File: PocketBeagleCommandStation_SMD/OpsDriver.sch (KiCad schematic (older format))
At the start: 0 parts

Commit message: Working on PocketBeagleCommandStation_SMD.
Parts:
- added C?: 47 nf, symbol C_Small
- added C?: 1 uf, symbol C_Small
- added C? (x2): 100 nf, symbol C
- added C?: 47 uf, symbol CP1
- added C?: 1 uf, symbol C
- added R?: 0.005 Ohms, symbol R
- added R? (x3): 10K Ohms, symbol R
- added U?: DRV8873HPWPR, SOP65P640X120-25N, symbol DRV8873HPWPR
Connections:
- net A: now also U?.18 (OUT1_1), U?.19 (OUT1_2)
- net B: now also U?.14 (OUT2_1), U?.15 (OUT2_2)
- net BRAKE: now also U?.9 (DISABLE)
- net ENABLE: now also U?.7 (EN/IN1)
- net PowerIn: now also R?.1
- net SIGNAL: now also U?.8 (PH/IN2)
- new net: C?.1, U?.1 (DVDD), U?.6 (NOL)
- new net: R?.2, U?.11 (NSLEEP)
- new net: R?.2, U?.2 (NFAULT)
- new net: C?.2, U?.21 (VCP)
- new net: C?.2, U?.22 (CPH)
- new net: C?.1, U?.23 (CPL)
- new net: R?.1, U?.3 (MODE)
- new net +3V3: R?.1, R?.1
- new net GND: C?.2, C?.2, C?.2, C?.2, R?.2, U?.16 (SRC_1), U?.17 (SRC_2), U?.24 (GND), U?.25 (EP), U?.4 (SR), U?.5 (NITRIP)
- new net Sense_Neg: C?.1, C?.1, C?.1, C?.1, R?.2, U?.13 (VM_1), U?.20 (VM_2)
- no-connect marks 0 -> 2

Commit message: Continuing work on PocketBeagleCommandStation_SMD.
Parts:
- U4: renamed from U?; footprint SOP65P640X120-25N -> SOP65P640X120:SOP65P640X120-25N
- gave numbers to parts that had none: 10
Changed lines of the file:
@@
 LIBS:DRV8873HPWPR
 LIBS:DRV8801PWP
+LIBS:74ahc1g08
+LIBS:mcp9701at
 LIBS:PocketBeagleCommandStation_SMD-cache
 EELAYER 25 0
@@
 Sense_Neg
 $Comp
-L DRV8873HPWPR U?
+L DRV8873HPWPR U4
 U 1 1 606FD60F
 P 3550 1800
-F 0 "U?" H 4800 2100 50  0000 L CNN
+F 0 "U4" H 4800 2100 50  0000 L CNN
 F 1 "DRV8873HPWPR" H 4800 2000 50  0000 L CNN
-F 2 "SOP65P640X120-25N" H 4800 1900 50  0001 L CNN
+F 2 "SOP65P640X120:SOP65P640X120-25N" H 4800 1900 50  0001 L CNN
 F 3 "http://www.ti.com/lit/ds/symlink/drv8873.pdf" H 4800 1800 50  0001 L CNN
 F 4 "Motor / Motion / Ignition Controllers & Drivers 10A H-Bridge Motor Driver with Integrated Current Sensing and Current Sense Output" H 4800 1700 50  0001 L CNN "Description"
@@
 $EndComp
 $Comp
-L GND #PWR?
+L GND #PWR028
 U 1 1 6070432B
 P 5250 1800
-F 0 "#PWR?" H 5250 1550 50  0001 C CNN
+F 0 "#PWR028" H 5250 1550 50  0001 C CNN
 F 1 "GND" H 5250 1650 50  0000 C CNN
 F 2 "" H 5250 1800 50  0001 C CNN
@@
 $EndComp
 $Comp
-L GND #PWR?
+L GND #PWR029
 U 1 1 60704370
 P 4250 3550
-F 0 "#PWR?" H 4250 3300 50  0001 C CNN
+F 0 "#PWR029" H 4250 3300 50  0001 C CNN
 F 1 "GND" H 4250 3400 50  0000 C CNN
 F 2 "" H 4250 3550 50  0001 C CNN
@@
 $EndComp
 $Comp
-L R R?
+L R R17
 U 1 1 607043BF
 P 5800 1550
-F 0 "R?" V 5880 1550 50  0000 C CNN
+F 0 "R17" V 5880 1550 50  0000 C CNN
 F 1 "0.005 Ohms" V 5800 1550 50  0000 C CNN
 F 2 "" V 5730 1550 50  0001 C CNN
@@
 Local_VDD
 $Comp
-L C_Small C?
+L C_Small C11
 U 1 1 607044D9
 P 5100 1950
-F 0 "C?" H 5110 2020 50  0000 L CNN
+F 0 "C11" H 5110 2020 50  0000 L CNN
 F 1 "47 nf" H 5110 1870 50  0000 L CNN
 F 2 "" H 5100 1950 50  0001 C CNN
@@
 $EndComp
 $Comp
-L C_Small C?
+L C_Small C12
 U 1 1 6070454C
 P 5250 2100
-F 0 "C?" H 5260 2170 50  0000 L CNN
+F 0 "C12" H 5260 2170 50  0000 L CNN
 F 1 "1 uf" H 5260 2020 50  0000 L CNN
 F 2 "" H 5250 2100 50  0001 C CNN
@@
 $EndComp
 $Comp
-L C C?
+L C C13
 U 1 1 607045D9
 P 5800 2450
-F 0 "C?" H 5825 2550 50  0000 L CNN
+F 0 "C13" H 5825 2550 50  0000 L CNN
 F 1 "100 nf" H 5825 2350 50  0000 L CNN
 F 2 "" H 5838 2300 50  0001 C CNN
@@
 $EndComp
 $Comp
-L C C?
+L C C14
 U 1 1 607045FC
 P 6150 2450
-F 0 "C?" H 6175 2550 50  0000 L CNN
+F 0 "C14" H 6175 2550 50  0000 L CNN
 F 1 "100 nf" H 6175 2350 50  0000 L CNN
 F 2 "" H 6188 2300 50  0001 C CNN
@@
 $EndComp
 $Comp
-L CP1 C?
+L CP1 C15
 U 1 1 60704621
 P 6500 2450
-F 0 "C?" H 6525 2550 50  0000 L CNN
+F 0 "C15" H 6525 2550 50  0000 L CNN
 F 1 "47 uf" H 6525 2350 50  0000 L CNN
 F 2 "" H 6500 2450 50  0001 C CNN
@@
 $EndComp
 $Comp
-L GND #PWR?
+L GND #PWR030
 U 1 1 60704783
 P 6150 2750
-F 0 "#PWR?" H 6150 2500 50  0001 C CNN
+F 0 "#PWR030" H 6150 2500 50  0001 C CNN
 F 1 "GND" H 6150 2600 50  0000 C CNN
 F 2 "" H 6150 2750 50  0001 C CNN
@@
 $EndComp
 $Comp
-L GND #PWR?
+L GND #PWR031
 U 1 1 60704831
 P 5300 2550
-F 0 "#PWR?" H 5300 2300 50  0001 C CNN
+F 0 "#PWR031" H 5300 2300 50  0001 C CNN
 F 1 "GND" H 5300 2400 50  0000 C CNN
 F 2 "" H 5300 2550 50  0001 C CNN
@@
 NoConn ~ 3550 2900
 $Comp
-L C C?
+L C C10
 U 1 1 607048DD
 P 3000 2000
-F 0 "C?" H 3025 2100 50  0000 L CNN
+F 0 "C10" H 3025 2100 50  0000 L CNN
 F 1 "1 uf" H 3025 1900 50  0000 L CNN
 F 2 "" H 3038 1850 50  0001 C CNN
@@
 $EndComp
 $Comp
-L GND #PWR?
+L GND #PWR032
 U 1 1 6070495B
 P 3000 2250
-F 0 "#PWR?" H 3000 2000 50  0001 C CNN
+F 0 "#PWR032" H 3000 2000 50  0001 C CNN
 F 1 "GND" H 3000 2100 50  0000 C CNN
 F 2 "" H 3000 2250 50  0001 C CNN
@@
 $EndComp
 $Comp
-L R R?
+L R R16
 U 1 1 60704A49
 P 3500 1450
-F 0 "R?" V 3580 1450 50  0000 C CNN
+F 0 "R16" V 3580 1450 50  0000 C CNN
 F 1 "10K Ohms" V 3500 1450 50  0000 C CNN
 F 2 "" V 3430 1450 50  0001 C CNN
@@
 $EndComp
 $Comp
-L R R?
+L R R15
 U 1 1 60704A7E
 P 3400 1450
-F 0 "R?" V 3480 1450 50  0000 C CNN
+F 0 "R15" V 3480 1450 50  0000 C CNN
 F 1 "10K Ohms" V 3400 1450 50  0000 C CNN
 F 2 "" V 3330 1450 50  0001 C CNN
@@
 $EndComp
 $Comp
-L +3.3V #PWR?
+L +3.3V #PWR033
 U 1 1 60707495
 P 3400 1100
-F 0 "#PWR?" H 3400 950 50  0001 C CNN
+F 0 "#PWR033" H 3400 950 50  0001 C CNN
 F 1 "+3.3V" H 3400 1240 50  0000 C CNN
 F 2 "" H 3400 1100 50  0001 C CNN
@@
 $EndComp
 $Comp
-L R R?
+L R R14
 U 1 1 6070758B
 P 2600 2150
-F 0 "R?" V 2680 2150 50  0000 C CNN
+F 0 "R14" V 2680 2150 50  0000 C CNN
 F 1 "10K Ohms" V 2600 2150 50  0000 C CNN
 F 2 "" V 2530 2150 50  0001 C CNN
@@
 $EndComp
 $Comp
-L GND #PWR?
+L GND #PWR034
 U 1 1 607075FE
 P 2600 2850
-F 0 "#PWR?" H 2600 2600 50  0001 C CNN
+F 0 "#PWR034" H 2600 2600 50  0001 C CNN
 F 1 "GND" H 2600 2700 50  0000 C CNN
 F 2 "" H 2600 2850 50  0001 C CNN
@@
 	5100 2350 5000 2350
 Wire Wire Line
-	5000 2300 5000 2350
-Wire Wire Line
-	5000 2350 5000 2400
+	5000 2300 5000 2400
 Wire Wire Line
 	5000 2300 4950 2300
@@
 	5100 2750 5000 2750
 Wire Wire Line
-	5000 2700 5000 2750
-Wire Wire Line
-	5000 2750 5000 2800
+	5000 2700 5000 2800
 Wire Wire Line
 	5000 2700 4950 2700
@@
 Connection ~ 5000 2750
 Wire Wire Line
-	4950 2200 5550 2200
-Wire Wire Line
-	5550 2200 5650 2200
-Wire Wire Line
-	5550 2200 5550 2300
-Wire Wire Line
-	5550 2300 5550 2900
+	5650 2200 4950 2200
+Wire Wire Line
+	5550 2200 5550 2900
 Wire Wire Line
 	5550 2900 4950 2900
@@
 	4250 3400 4250 3550
 Wire Wire Line
-	6050 1550 6000 1550
-Wire Wire Line
-	6000 1550 5950 1550
-Wire Wire Line
-	5650 2200 5650 2100
-Wire Wire Line
-	5650 2100 5650 1950
-Wire Wire Line
-	5650 1950 5650 1550
+	5950 1550 6050 1550
+Wire Wire Line
+	5650 1550 5650 2200
 Connection ~ 5550 2200
 Wire Wire Line
@@
 Connection ~ 5650 2100
 Wire Wire Line
-	5550 2300 5800 2300
-Wire Wire Line
-	5800 2300 6150 2300
-Wire Wire Line
-	6150 2300 6500 2300
+	5550 2300 6500 2300
 Connection ~ 6150 2300
 Connection ~ 5550 2300
 Connection ~ 5800 2300
 Wire Wire Line
-	5800 2600 6150 2600
-Wire Wire Line
-	6150 2600 6500 2600
+	5800 2600 6500 2600
 Connection ~ 6150 2600
 Wire Wire Line
@@
 	4950 2500 5050 2500
 Wire Wire Line
-	5050 2500 5050 2550
-Wire Wire Line
-	5050 2550 5050 2600
+	5050 2500 5050 2600
 Wire Wire Line
 	5050 2600 4950 2600
@@
 Connection ~ 5050 2550
 Wire Wire Line
-	3000 1800 3250 1800
-Wire Wire Line
-	3250 1800 3550 1800
+	3000 1800 3550 1800
 Wire Wire Line
 	3250 1800 3250 2300
@@
 Connection ~ 3250 1800
 Wire Wire Line
-	3000 2150 3000 2200
-Wire Wire Line
-	3000 2200 3000 2250
+	3000 2150 3000 2250
 Wire Wire Line
 	3500 1600 3500 1900
@@
 	3400 2800 3550 2800
 Wire Wire Line
-	3400 1100 3400 1150
-Wire Wire Line
-	3400 1150 3400 1300
+	3400 1100 3400 1300
 Wire Wire Line
 	3500 1300 3500 1150
@@
 	3450 2100 3450 2200
 Wire Wire Line
-	3000 2200 3450 2200
-Wire Wire Line
-	3450 2200 3550 2200
+	3000 2200 3550 2200
 Connection ~ 3000 2200
 Connection ~ 3450 2200

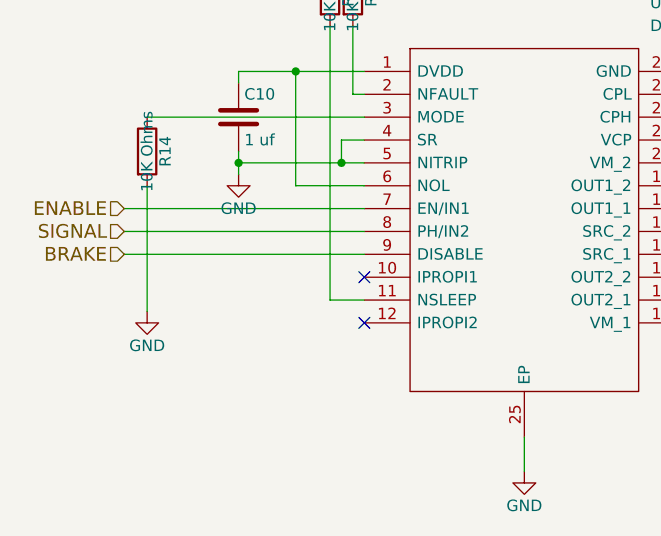
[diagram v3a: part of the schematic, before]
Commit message: Continuing work on the SMD version of PocketBeagleCommandStation.
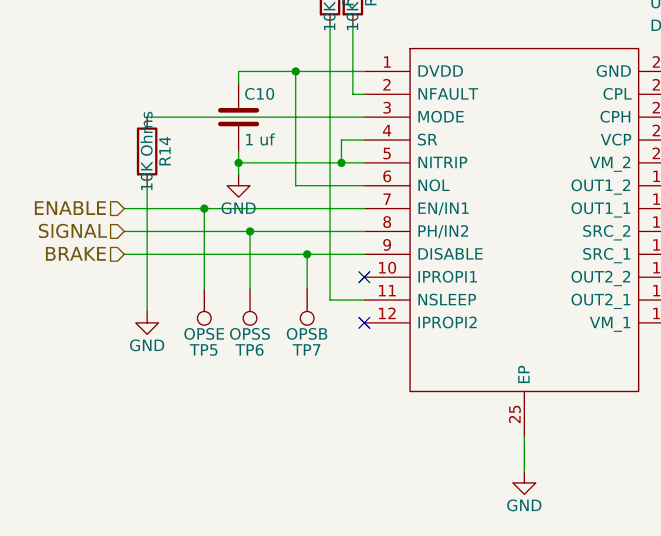
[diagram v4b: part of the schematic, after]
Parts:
- added TP5: OPSE, symbol TEST_1P
- added TP6: OPSS, symbol TEST_1P
- added TP7: OPSB, symbol TEST_1P
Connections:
- net BRAKE: now also TP7.1
- net ENABLE: now also TP5.1
- net SIGNAL: now also TP6.1
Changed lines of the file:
@@
 LIBS:74ahc1g08
 LIBS:mcp9701at
+LIBS:INA2180A1IDGKR
 LIBS:PocketBeagleCommandStation_SMD-cache
 EELAYER 25 0
@@
 $EndComp
 $Comp
-L GND #PWR028
+L GND #PWR37
 U 1 1 6070432B
 P 5250 1800
-F 0 "#PWR028" H 5250 1550 50  0001 C CNN
+F 0 "#PWR37" H 5250 1550 50  0001 C CNN
 F 1 "GND" H 5250 1650 50  0000 C CNN
 F 2 "" H 5250 1800 50  0001 C CNN
@@
 $EndComp
 $Comp
-L GND #PWR029
+L GND #PWR36
 U 1 1 60704370
 P 4250 3550
-F 0 "#PWR029" H 4250 3300 50  0001 C CNN
+F 0 "#PWR36" H 4250 3300 50  0001 C CNN
 F 1 "GND" H 4250 3400 50  0000 C CNN
 F 2 "" H 4250 3550 50  0001 C CNN
@@
 $EndComp
 $Comp
-L GND #PWR030
+L GND #PWR39
 U 1 1 60704783
 P 6150 2750
-F 0 "#PWR030" H 6150 2500 50  0001 C CNN
+F 0 "#PWR39" H 6150 2500 50  0001 C CNN
 F 1 "GND" H 6150 2600 50  0000 C CNN
 F 2 "" H 6150 2750 50  0001 C CNN
@@
 $EndComp
 $Comp
-L GND #PWR031
+L GND #PWR38
 U 1 1 60704831
 P 5300 2550
-F 0 "#PWR031" H 5300 2300 50  0001 C CNN
+F 0 "#PWR38" H 5300 2300 50  0001 C CNN
 F 1 "GND" H 5300 2400 50  0000 C CNN
 F 2 "" H 5300 2550 50  0001 C CNN
@@
 $EndComp
 $Comp
-L GND #PWR032
+L GND #PWR34
 U 1 1 6070495B
 P 3000 2250
-F 0 "#PWR032" H 3000 2000 50  0001 C CNN
+F 0 "#PWR34" H 3000 2000 50  0001 C CNN
 F 1 "GND" H 3000 2100 50  0000 C CNN
 F 2 "" H 3000 2250 50  0001 C CNN
@@
 $EndComp
 $Comp
-L +3.3V #PWR033
+L +3.3V #PWR35
 U 1 1 60707495
 P 3400 1100
-F 0 "#PWR033" H 3400 950 50  0001 C CNN
+F 0 "#PWR35" H 3400 950 50  0001 C CNN
 F 1 "+3.3V" H 3400 1240 50  0000 C CNN
 F 2 "" H 3400 1100 50  0001 C CNN
@@
 $EndComp
 $Comp
-L GND #PWR034
+L GND #PWR33
 U 1 1 607075FE
 P 2600 2850
-F 0 "#PWR034" H 2600 2600 50  0001 C CNN
+F 0 "#PWR33" H 2600 2600 50  0001 C CNN
 F 1 "GND" H 2600 2700 50  0000 C CNN
 F 2 "" H 2600 2850 50  0001 C CNN
@@
 	1    0    0    -1
 $EndComp
+$Comp
+L TEST_1P TP7
+U 1 1 60742F6B
+P 3300 2750
+F 0 "TP7" H 3300 3020 50  0000 C CNN
+F 1 "OPSB" H 3300 2950 50  0000 C CNN
+F 2 "" H 3500 2750 50  0001 C CNN
+F 3 "" H 3500 2750 50  0001 C CNN
+	1    3300 2750
+	-1   0    0    1
+$EndComp
+$Comp
+L TEST_1P TP6
+U 1 1 60743082
+P 3050 2750
+F 0 "TP6" H 3050 3020 50  0000 C CNN
+F 1 "OPSS" H 3050 2950 50  0000 C CNN
+F 2 "" H 3250 2750 50  0001 C CNN
+F 3 "" H 3250 2750 50  0001 C CNN
+	1    3050 2750
+	-1   0    0    1
+$EndComp
+$Comp
+L TEST_1P TP5
+U 1 1 607430B7
+P 2850 2750
+F 0 "TP5" H 2850 3020 50  0000 C CNN
+F 1 "OPSE" H 2850 2950 50  0000 C CNN
+F 2 "" H 3050 2750 50  0001 C CNN
+F 3 "" H 3050 2750 50  0001 C CNN
+	1    2850 2750
+	-1   0    0    1
+$EndComp
 Wire Wire Line
 	2500 2400 3550 2400
@@
 Connection ~ 3000 2200
 Connection ~ 3450 2200
+Wire Wire Line
+	2850 2750 2850 2400
+Connection ~ 2850 2400
+Wire Wire Line
+	3050 2750 3050 2500
+Connection ~ 3050 2500
+Wire Wire Line
+	3300 2750 3300 2600
+Connection ~ 3300 2600
 $EndSCHEMATC

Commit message: Continuing with the PocketBeagle Command Station, SMD version.
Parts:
- C10, C12: footprint (none) -> Capacitors_SMD:C_0603; Mouser Part Number (none) -> 963-GMK107AB7105KAHT
- C11: footprint (none) -> Capacitors_SMD:C_0603; Mouser Part Number (none) -> 963-GMK107BJ473KAHT
- C13: footprint (none) -> Capacitors_SMD:C_0603; Mouser Part Nmber (none) -> 603-CC603KPX7R9BB104
- C14: footprint (none) -> Capacitors_SMD:C_0603; Mouser Part Number (none) -> 603-CC603KPX7R9BB104
- C15: footprint (none) -> Capacitors_SMD:CP_Elec_6.3x5.3; Mouser Part Number (none) -> 710-865080543009
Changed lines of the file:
@@
 F 0 "C11" H 5110 2020 50  0000 L CNN
 F 1 "47 nf" H 5110 1870 50  0000 L CNN
-F 2 "" H 5100 1950 50  0001 C CNN
+F 2 "Capacitors_SMD:C_0603" H 5100 1950 50  0001 C CNN
 F 3 "" H 5100 1950 50  0001 C CNN
+F 4 "963-GMK107BJ473KAHT" H 5100 1950 60  0001 C CNN "Mouser Part Number"
 	1    5100 1950
 	1    0    0    -1
@@
 F 0 "C12" H 5260 2170 50  0000 L CNN
 F 1 "1 uf" H 5260 2020 50  0000 L CNN
-F 2 "" H 5250 2100 50  0001 C CNN
+F 2 "Capacitors_SMD:C_0603" H 5250 2100 50  0001 C CNN
 F 3 "" H 5250 2100 50  0001 C CNN
+F 4 "963-GMK107AB7105KAHT" H 5250 2100 60  0001 C CNN "Mouser Part Number"
 	1    5250 2100
 	0    1    1    0
@@
 F 0 "C13" H 5825 2550 50  0000 L CNN
 F 1 "100 nf" H 5825 2350 50  0000 L CNN
-F 2 "" H 5838 2300 50  0001 C CNN
+F 2 "Capacitors_SMD:C_0603" H 5838 2300 50  0001 C CNN
 F 3 "" H 5800 2450 50  0001 C CNN
+F 4 "603-CC603KPX7R9BB104" H 5800 2450 60  0001 C CNN "Mouser Part Nmber"
 	1    5800 2450
 	1    0    0    -1
@@
 F 0 "C14" H 6175 2550 50  0000 L CNN
 F 1 "100 nf" H 6175 2350 50  0000 L CNN
-F 2 "" H 6188 2300 50  0001 C CNN
+F 2 "Capacitors_SMD:C_0603" H 6188 2300 50  0001 C CNN
 F 3 "" H 6150 2450 50  0001 C CNN
+F 4 "603-CC603KPX7R9BB104" H 6150 2450 60  0001 C CNN "Mouser Part Number"
 	1    6150 2450
 	1    0    0    -1
@@
 F 0 "C15" H 6525 2550 50  0000 L CNN
 F 1 "47 uf" H 6525 2350 50  0000 L CNN
-F 2 "" H 6500 2450 50  0001 C CNN
+F 2 "Capacitors_SMD:CP_Elec_6.3x5.3" H 6500 2450 50  0001 C CNN
 F 3 "" H 6500 2450 50  0001 C CNN
+F 4 "710-865080543009" H 6500 2450 60  0001 C CNN "Mouser Part Number"
 	1    6500 2450
 	1    0    0    -1
@@
 F 0 "C10" H 3025 2100 50  0000 L CNN
 F 1 "1 uf" H 3025 1900 50  0000 L CNN
-F 2 "" H 3038 1850 50  0001 C CNN
+F 2 "Capacitors_SMD:C_0603" H 3038 1850 50  0001 C CNN
 F 3 "" H 3000 2000 50  0001 C CNN
+F 4 "963-GMK107AB7105KAHT" H 3000 2000 60  0001 C CNN "Mouser Part Number"
 	1    3000 2000
 	1    0    0    -1

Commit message: Continuing work on PocketBeagleCommandStation_SMD.
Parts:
- R14, R16: value 10K Ohms -> 10K; footprint (none) -> Resistors_SMD:R_0603; Mouser Part Number (none) -> 279-CRGCQ0603F10K
- R15: value 10K Ohms -> 10K; footprint (none) -> Resistors_SMD:R_0603; Mouser Part Numer (none) -> 279-CRGCQ0603F10K
- R17: value 0.005 Ohms -> 0.005 1%; footprint (none) -> Resistors_SMD:R_0612; Mouser Part Number (none) -> 71-WSKW0612L5000FEA
- TP5, TP6, TP7: footprint (none) -> Measurement_Points:Measurement_Point_Round-SMD-Pad_Big
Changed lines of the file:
@@
 $EndComp
 $Comp
-L GND #PWR036
+L GND #PWR037
 U 1 1 6070432B
 P 5250 1800
-F 0 "#PWR036" H 5250 1550 50  0001 C CNN
+F 0 "#PWR037" H 5250 1550 50  0001 C CNN
 F 1 "GND" H 5250 1650 50  0000 C CNN
 F 2 "" H 5250 1800 50  0001 C CNN
@@
 $EndComp
 $Comp
-L GND #PWR037
+L GND #PWR038
 U 1 1 60704370
 P 4250 3550
-F 0 "#PWR037" H 4250 3300 50  0001 C CNN
+F 0 "#PWR038" H 4250 3300 50  0001 C CNN
 F 1 "GND" H 4250 3400 50  0000 C CNN
 F 2 "" H 4250 3550 50  0001 C CNN
@@
 P 5800 1550
 F 0 "R17" V 5880 1550 50  0000 C CNN
-F 1 "0.005 Ohms" V 5800 1550 50  0000 C CNN
-F 2 "" V 5730 1550 50  0001 C CNN
+F 1 "0.005 1%" V 5800 1550 50  0000 C CNN
+F 2 "Resistors_SMD:R_0612" V 5730 1550 50  0001 C CNN
 F 3 "" H 5800 1550 50  0001 C CNN
+F 4 "71-WSKW0612L5000FEA" V 5800 1550 60  0001 C CNN "Mouser Part Number"
 	1    5800 1550
 	0    1    1    0
@@
 $EndComp
 $Comp
-L GND #PWR038
+L GND #PWR039
 U 1 1 60704783
 P 6150 2750
-F 0 "#PWR038" H 6150 2500 50  0001 C CNN
+F 0 "#PWR039" H 6150 2500 50  0001 C CNN
 F 1 "GND" H 6150 2600 50  0000 C CNN
 F 2 "" H 6150 2750 50  0001 C CNN
@@
 $EndComp
 $Comp
-L GND #PWR039
+L GND #PWR040
 U 1 1 60704831
 P 5300 2550
-F 0 "#PWR039" H 5300 2300 50  0001 C CNN
+F 0 "#PWR040" H 5300 2300 50  0001 C CNN
 F 1 "GND" H 5300 2400 50  0000 C CNN
 F 2 "" H 5300 2550 50  0001 C CNN
@@
 $EndComp
 $Comp
-L GND #PWR040
+L GND #PWR041
 U 1 1 6070495B
 P 3000 2250
-F 0 "#PWR040" H 3000 2000 50  0001 C CNN
+F 0 "#PWR041" H 3000 2000 50  0001 C CNN
 F 1 "GND" H 3000 2100 50  0000 C CNN
 F 2 "" H 3000 2250 50  0001 C CNN
@@
 P 3500 1450
 F 0 "R16" V 3580 1450 50  0000 C CNN
-F 1 "10K Ohms" V 3500 1450 50  0000 C CNN
-F 2 "" V 3430 1450 50  0001 C CNN
+F 1 "10K" V 3500 1450 50  0000 C CNN
+F 2 "Resistors_SMD:R_0603" V 3430 1450 50  0001 C CNN
 F 3 "" H 3500 1450 50  0001 C CNN
+F 4 "279-CRGCQ0603F10K" V 3500 1450 60  0001 C CNN "Mouser Part Number"
 	1    3500 1450
 	1    0    0    -1
@@
 P 3400 1450
 F 0 "R15" V 3480 1450 50  0000 C CNN
-F 1 "10K Ohms" V 3400 1450 50  0000 C CNN
-F 2 "" V 3330 1450 50  0001 C CNN
+F 1 "10K" V 3400 1450 50  0000 C CNN
+F 2 "Resistors_SMD:R_0603" V 3330 1450 50  0001 C CNN
 F 3 "" H 3400 1450 50  0001 C CNN
+F 4 "279-CRGCQ0603F10K" V 3400 1450 60  0001 C CNN "Mouser Part Numer"
 	1    3400 1450
 	1    0    0    -1
 $EndComp
 $Comp
-L +3.3V #PWR041
+L +3.3V #PWR042
 U 1 1 60707495
 P 3400 1100
-F 0 "#PWR041" H 3400 950 50  0001 C CNN
+F 0 "#PWR042" H 3400 950 50  0001 C CNN
 F 1 "+3.3V" H 3400 1240 50  0000 C CNN
 F 2 "" H 3400 1100 50  0001 C CNN
@@
 P 2600 2150
 F 0 "R14" V 2680 2150 50  0000 C CNN
-F 1 "10K Ohms" V 2600 2150 50  0000 C CNN
-F 2 "" V 2530 2150 50  0001 C CNN
+F 1 "10K" V 2600 2150 50  0000 C CNN
+F 2 "Resistors_SMD:R_0603" V 2530 2150 50  0001 C CNN
 F 3 "" H 2600 2150 50  0001 C CNN
+F 4 "279-CRGCQ0603F10K" V 2600 2150 60  0001 C CNN "Mouser Part Number"
 	1    2600 2150
 	1    0    0    -1
 $EndComp
 $Comp
-L GND #PWR042
+L GND #PWR043
 U 1 1 607075FE
 P 2600 2850
-F 0 "#PWR042" H 2600 2600 50  0001 C CNN
+F 0 "#PWR043" H 2600 2600 50  0001 C CNN
 F 1 "GND" H 2600 2700 50  0000 C CNN
 F 2 "" H 2600 2850 50  0001 C CNN
@@
 F 0 "TP7" H 3300 3020 50  0000 C CNN
 F 1 "OPSB" H 3300 2950 50  0000 C CNN
-F 2 "" H 3500 2750 50  0001 C CNN
+F 2 "Measurement_Points:Measurement_Point_Round-SMD-Pad_Big" H 3500 2750 50  0001 C CNN
 F 3 "" H 3500 2750 50  0001 C CNN
 	1    3300 2750
@@
 F 0 "TP6" H 3050 3020 50  0000 C CNN
 F 1 "OPSS" H 3050 2950 50  0000 C CNN
-F 2 "" H 3250 2750 50  0001 C CNN
+F 2 "Measurement_Points:Measurement_Point_Round-SMD-Pad_Big" H 3250 2750 50  0001 C CNN
 F 3 "" H 3250 2750 50  0001 C CNN
 	1    3050 2750
@@
 F 0 "TP5" H 2850 3020 50  0000 C CNN
 F 1 "OPSE" H 2850 2950 50  0000 C CNN
-F 2 "" H 3050 2750 50  0001 C CNN
+F 2 "Measurement_Points:Measurement_Point_Round-SMD-Pad_Big" H 3050 2750 50  0001 C CNN
 F 3 "" H 3050 2750 50  0001 C CNN
 	1    2850 2750
